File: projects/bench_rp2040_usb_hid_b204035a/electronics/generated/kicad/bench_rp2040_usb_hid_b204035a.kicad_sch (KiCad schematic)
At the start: 10 parts, among them J1 USB-C POWER, J2 SWD 10-pin, U1 3V3 LDO, U2 RP2040, U3 2MB QSPI, X1 12MHz XTAL

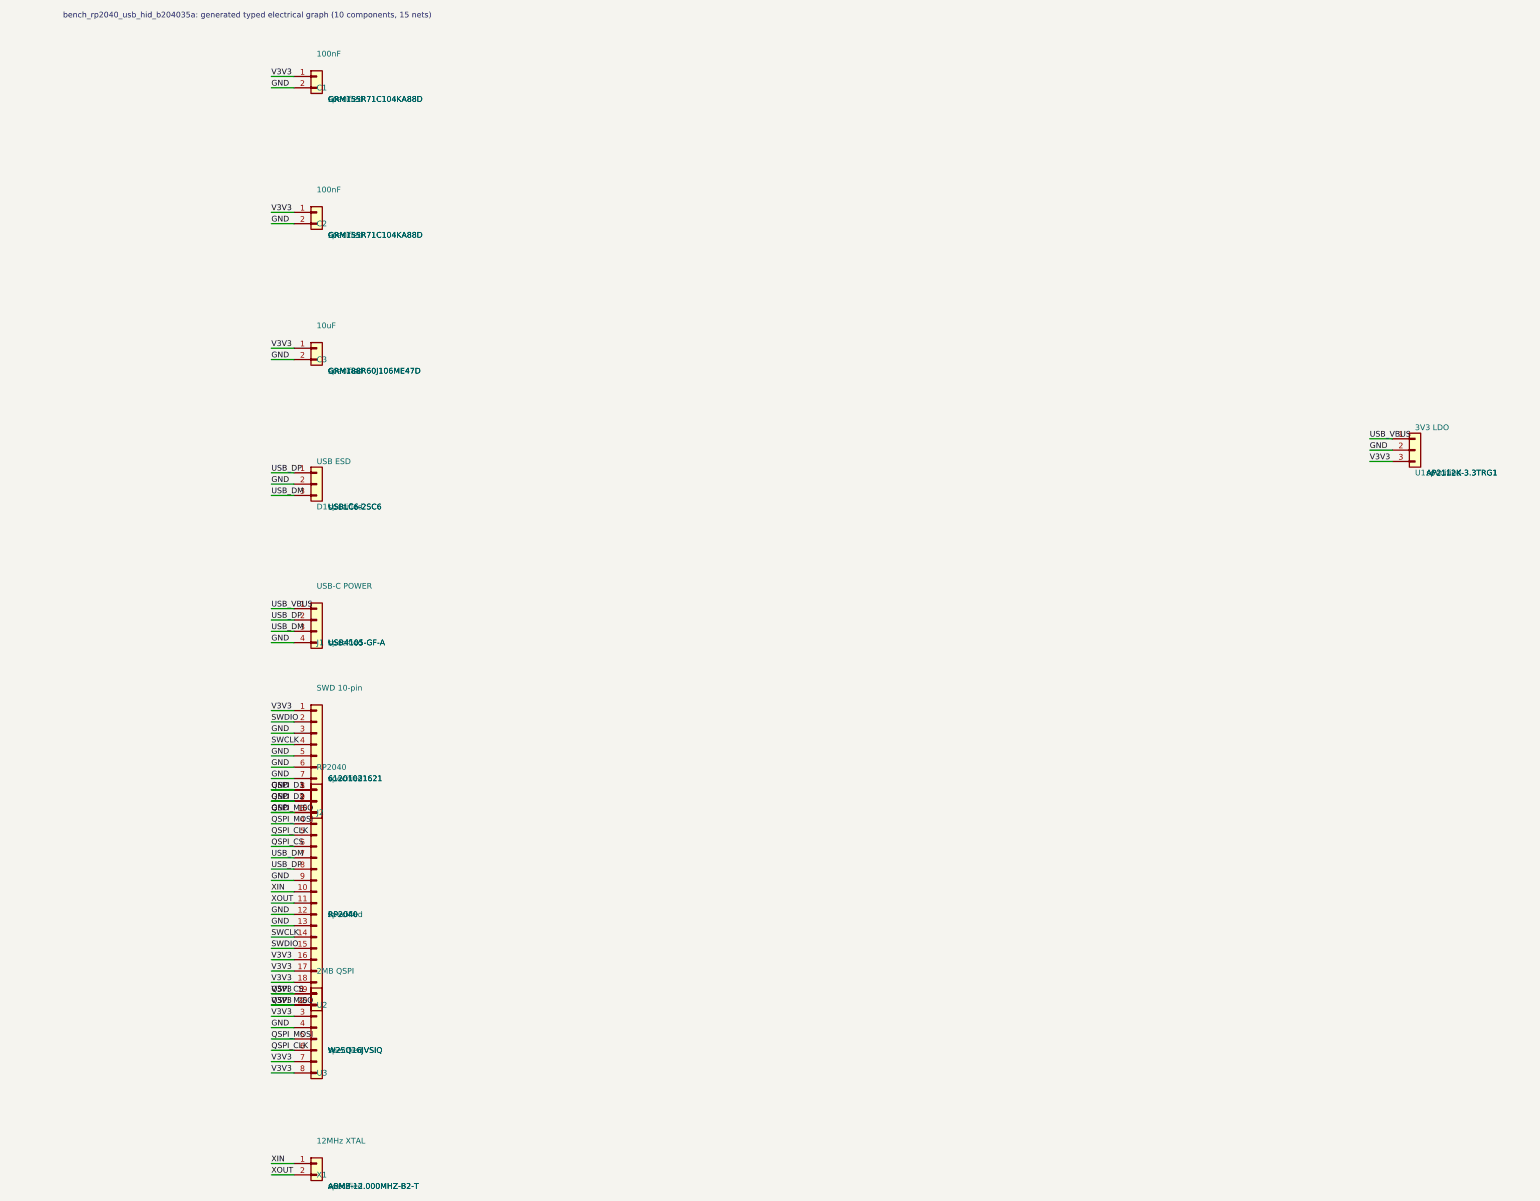
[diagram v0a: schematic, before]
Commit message: chore: refresh rp2040 benchmark evidence
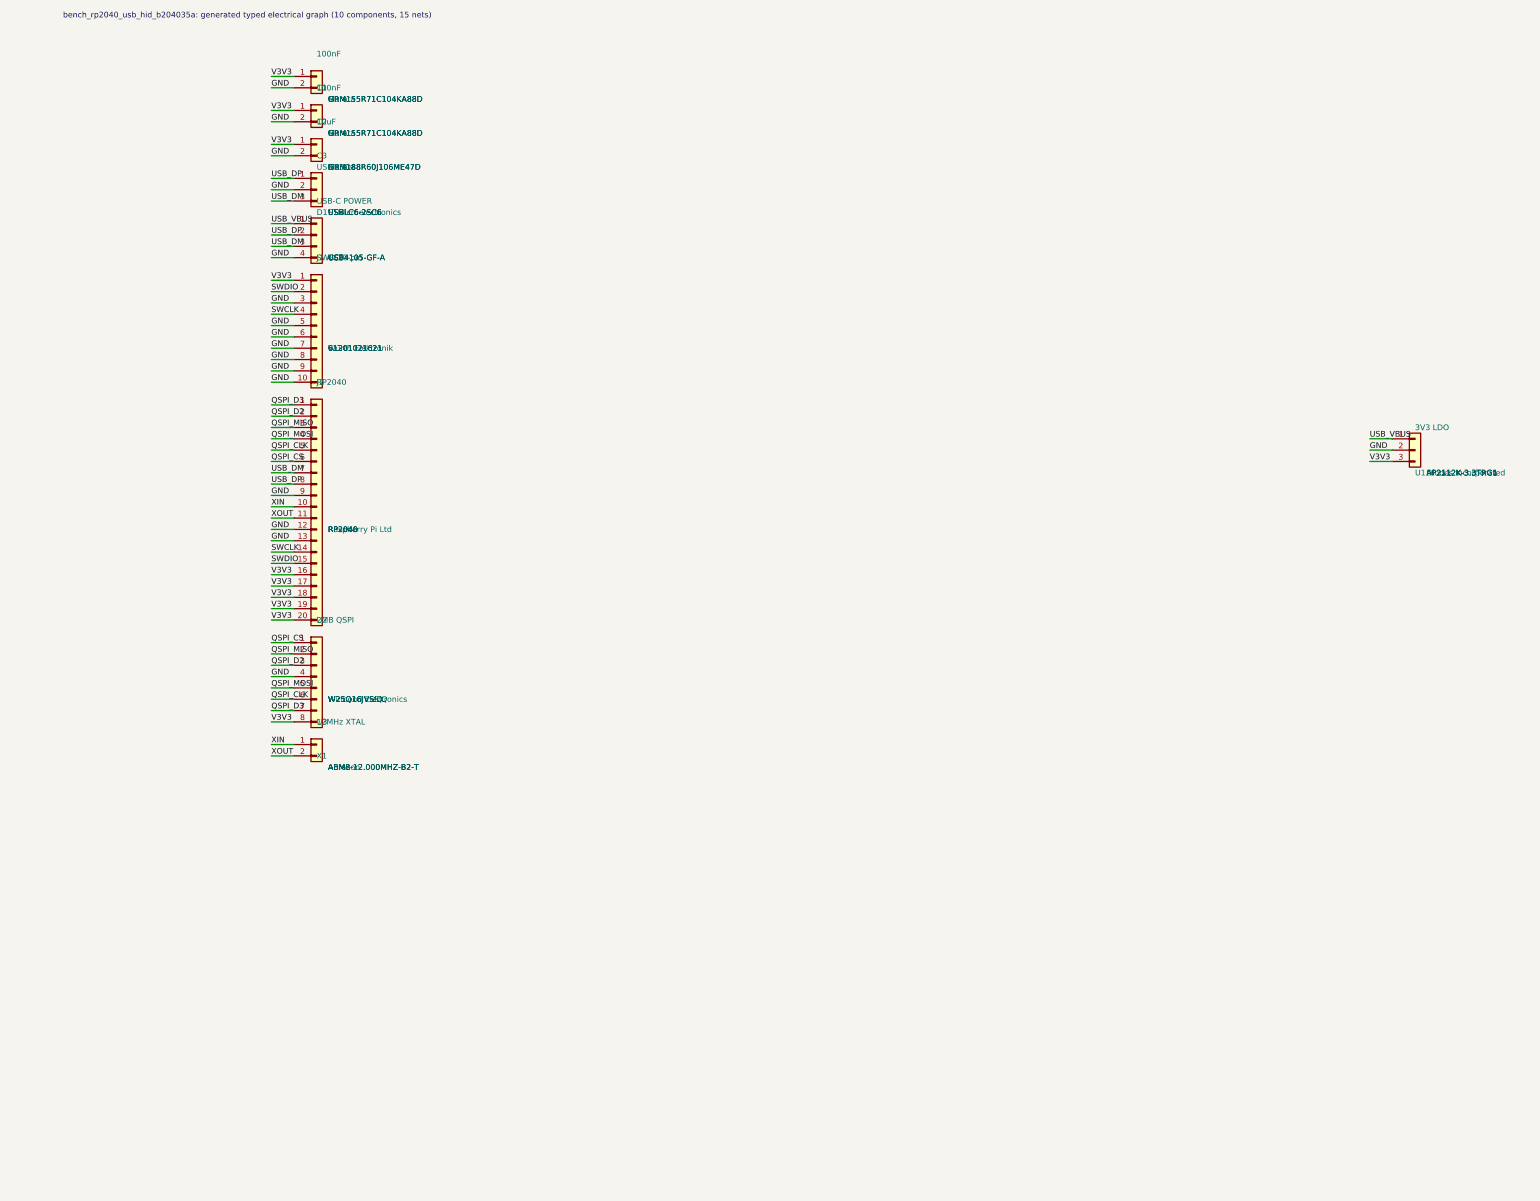
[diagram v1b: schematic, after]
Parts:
- C1, C2: footprint 0402 -> Capacitor_SMD:C_0402_1005Metric; Manufacturer specified -> Murata
- C3: footprint 0603 -> Capacitor_SMD:C_0603_1608Metric; Manufacturer specified -> Murata
- D1: footprint SOT23-6 -> Package_TO_SOT_SMD:SOT-23-6; Manufacturer specified -> STMicroelectronics
- J1: footprint USB_C_16Pin -> Connector_USB:USB_C_GCT_USB4105; Manufacturer specified -> GCT
- J2: footprint PinHeader-2x5 -> Connector_PinHeader_2.54mm:PinHeader_2x05_P2.54mm_Vertical; Manufacturer specified -> Würth Elektronik
- U1: footprint SOT23-5 -> Package_TO_SOT_SMD:SOT-23-5; Manufacturer specified -> Diodes Incorporated
- U2: footprint QFN-56 -> Package_DFN_QFN:QFN-56-1EP_7x7mm_P0.4mm_EP3.2x3.2mm; Manufacturer specified -> Raspberry Pi Ltd
- U3: footprint SOIC-8 -> Package_SO:SOIC-8_3.9x4.9mm_P1.27mm; MPN W25Q16JVSIQ -> W25Q16JVSSIQ; Manufacturer specified -> Winbond Electronics
- X1: footprint HC-49S-SMD -> Crystal:Crystal_SMD_HC-49S; Manufacturer specified -> Abracon
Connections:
- net GND: no longer C1.1 (Pin_1), C2.1 (Pin_1), C3.1 (Pin_1), J2.1 (Pin_1), U1.3 (Pin_3), U2.1 (Pin_1), U2.16 (Pin_16), U2.17 (Pin_17), U2.18 (Pin_18), U2.19 (Pin_19), U2.2 (Pin_2), U2.20 (Pin_20), U2.3 (Pin_3), U2.6 (Pin_6), U3.1 (Pin_1), U3.2 (Pin_2), U3.3 (Pin_3), U3.7 (Pin_7), U3.8 (Pin_8)
- new net QSPI_CS: U2.6 (Pin_6), U3.1 (Pin_1)
- new net QSPI_D2: U2.2 (Pin_2), U3.3 (Pin_3)
- new net QSPI_D3: U2.1 (Pin_1), U3.7 (Pin_7)
- new net QSPI_MISO: U2.3 (Pin_3), U3.2 (Pin_2)
- new net V3V3: C1.1 (Pin_1), C2.1 (Pin_1), C3.1 (Pin_1), J2.1 (Pin_1), U1.3 (Pin_3), U2.16 (Pin_16), U2.17 (Pin_17), U2.18 (Pin_18), U2.19 (Pin_19), U2.20 (Pin_20), U3.8 (Pin_8)
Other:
- moved on the sheet: C2, C3, D1, J1, J2, U2, U3, X1
